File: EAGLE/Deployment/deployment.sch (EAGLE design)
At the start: 7 parts, among them J1 1935161, J2 1935161, J3 1935161, Q1 100V 14A

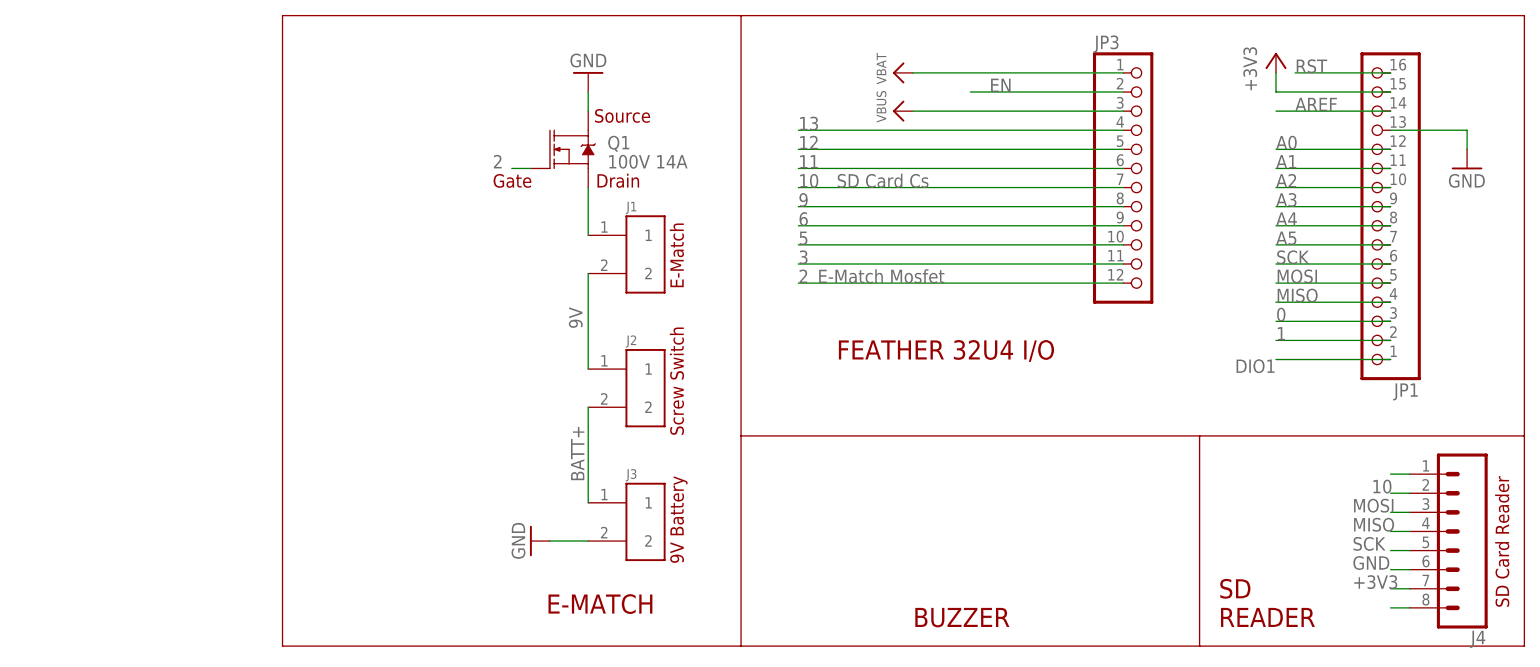
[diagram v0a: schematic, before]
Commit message: Fixed wiring of nichrome wire circit in the depolyment schematic
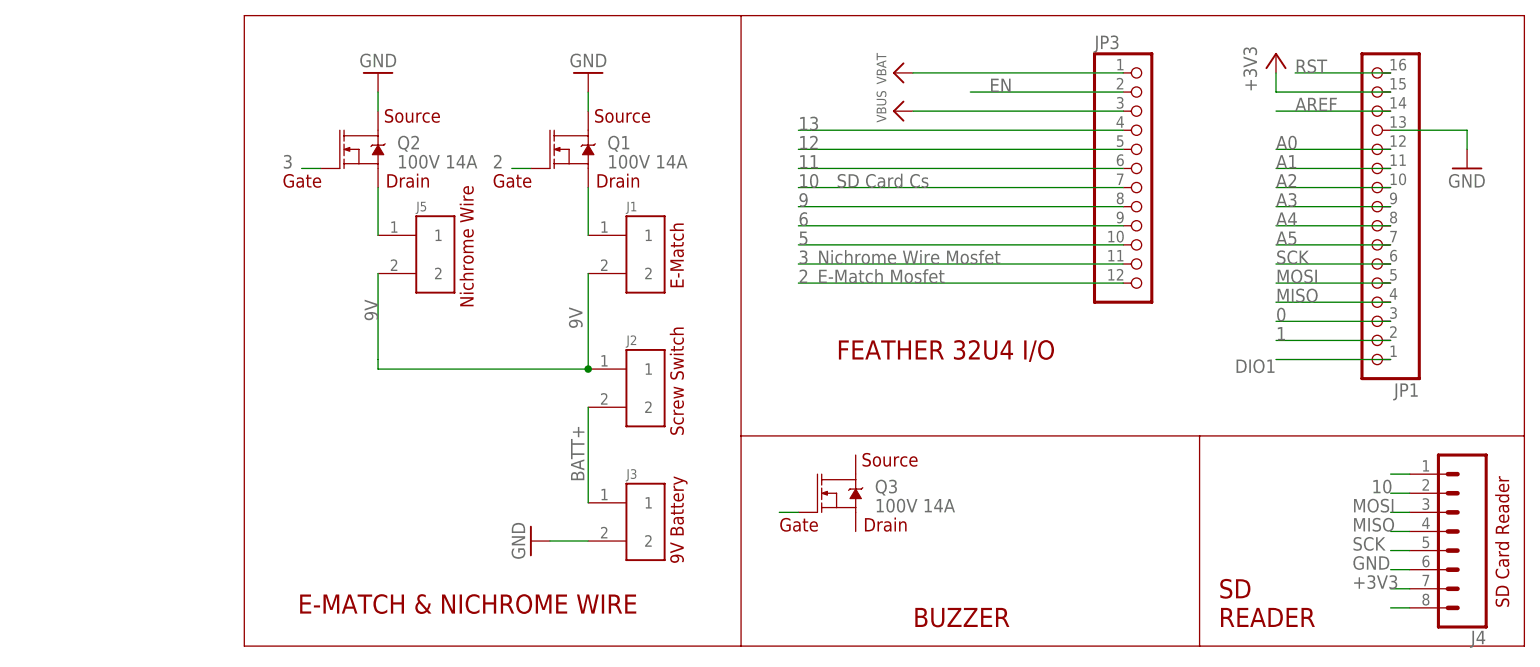
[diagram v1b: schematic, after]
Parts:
- added J5: 1935161, 1935161:1935161
- added Q2, Q3: 100V 14A, SparkFun-DiscreteSemi:MOSFET-NCH-FQP30N06L
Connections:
- new net 4: Q3.G
- new net N$2: J5.1, Q2.S
- net 3: now also Q2.G
- net 9V: now also J5.2
- net GND: now also Q2.D
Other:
- note added: "E-MATCH & NICHROME WIRE"
- note added: "Nichrome Wire"
- note added: "Nichrome Wire Mosfet"
- note removed: "E-MATCH"
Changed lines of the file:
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@@
 <?xml version="1.0" encoding="utf-8"?>
 <!DOCTYPE eagle SYSTEM "eagle.dtd">
-<eagle version="9.5.2">
+<eagle version="9.2.2">
 <drawing>
 <settings>
@@
 <part name="GND2" library="supply1" deviceset="GND" device=""/>
 <part name="J4" library="SparkFun-Connectors" library_urn="urn:adsk.eagle:library:513" deviceset="CONN_08" device="&quot;" package3d_urn="urn:adsk.eagle:package:38138/1"/>
+<part name="Q2" library="SparkFun-DiscreteSemi" library_urn="urn:adsk.eagle:library:514" deviceset="MOSFET-NCH" device="-FQP30N06L" package3d_urn="urn:adsk.eagle:package:38447/1" value="100V 14A"/>
+<part name="J5" library="1935161" deviceset="1935161" device="" value=""/>
+<part name="GND3" library="supply1" deviceset="GND" device=""/>
+<part name="Q3" library="SparkFun-DiscreteSemi" library_urn="urn:adsk.eagle:library:514" deviceset="MOSFET-NCH" device="-FQP30N06L" package3d_urn="urn:adsk.eagle:package:38447/1" value="100V 14A"/>
 </parts>
 <sheets>
@@
 <wire x1="127" y1="7.62" x2="127" y2="35.56" width="0.1524" layer="94"/>
 <wire x1="127" y1="7.62" x2="66.04" y2="7.62" width="0.1524" layer="94"/>
-<wire x1="66.04" y1="7.62" x2="5.08" y2="7.62" width="0.1524" layer="94"/>
-<wire x1="5.08" y1="7.62" x2="5.08" y2="91.44" width="0.1524" layer="94"/>
-<wire x1="5.08" y1="91.44" x2="66.04" y2="91.44" width="0.1524" layer="94"/>
+<wire x1="66.04" y1="7.62" x2="0" y2="7.62" width="0.1524" layer="94"/>
+<wire x1="0" y1="7.62" x2="0" y2="91.44" width="0.1524" layer="94"/>
+<wire x1="0" y1="91.44" x2="66.04" y2="91.44" width="0.1524" layer="94"/>
 <wire x1="66.04" y1="35.56" x2="66.04" y2="7.62" width="0.1524" layer="94"/>
-<text x="40.132" y="11.938" size="2.54" layer="94">E-MATCH</text>
+<text x="7.112" y="11.938" size="2.54" layer="94">E-MATCH &amp; NICHROME WIRE</text>
 <text x="78.74" y="45.72" size="2.54" layer="94">FEATHER 32U4 I/O</text>
 <text x="129.54" y="10.16" size="2.54" layer="94">SD
@@
 <text x="76.2" y="55.88" size="1.778" layer="95">E-Match Mosfet</text>
 <text x="78.74" y="68.58" size="1.778" layer="95">SD Card Cs</text>
+<text x="5.08" y="68.58" size="1.778" layer="94">Gate</text>
+<text x="18.542" y="77.216" size="1.778" layer="94">Source</text>
+<text x="18.796" y="68.58" size="1.778" layer="94">Drain</text>
+<text x="30.48" y="52.578" size="1.778" layer="94" rot="R90">Nichrome Wire</text>
+<text x="82.042" y="31.496" size="1.778" layer="94">Source</text>
+<text x="82.296" y="22.86" size="1.778" layer="94">Drain</text>
+<text x="71.12" y="22.86" size="1.778" layer="94">Gate</text>
+<text x="76.2" y="58.42" size="1.778" layer="95">Nichrome Wire Mosfet</text>
 </plain>
 <instances>
@@
 <attribute name="VALUE" x="165.1" y="35.306" size="1.778" layer="96" font="vector" rot="R180"/>
 <attribute name="NAME" x="165.1" y="9.652" size="1.778" layer="95" font="vector" rot="R180"/>
+</instance>
+<instance part="Q2" gate="NMOS" x="15.24" y="73.66" smashed="yes">
+<attribute name="NAME" x="20.32" y="73.66" size="1.778" layer="95" font="vector"/>
+<attribute name="VALUE" x="20.32" y="71.12" size="1.778" layer="96" font="vector"/>
+</instance>
+<instance part="J5" gate="G$1" x="25.4" y="59.69" smashed="yes">
+<attribute name="NAME" x="22.85451875" y="65.417340625" size="1.272740625" layer="95"/>
+<attribute name="VALUE" x="22.85191875" y="52.04576875" size="1.274040625" layer="96"/>
+</instance>
+<instance part="GND3" gate="1" x="17.78" y="83.82" smashed="yes" rot="R180">
+<attribute name="VALUE" x="20.32" y="86.36" size="1.778" layer="96" rot="R180"/>
+</instance>
+<instance part="Q3" gate="NMOS" x="78.74" y="27.94" smashed="yes">
+<attribute name="NAME" x="83.82" y="27.94" size="1.778" layer="95" font="vector"/>
+<attribute name="VALUE" x="83.82" y="25.4" size="1.778" layer="96" font="vector"/>
 </instance>
 </instances>
@@
 <label x="147.32" y="17.78" size="1.778" layer="95"/>
 </segment>
+<segment>
+<pinref part="GND3" gate="1" pin="GND"/>
+<pinref part="Q2" gate="NMOS" pin="D"/>
+<wire x1="17.78" y1="81.28" x2="17.78" y2="78.74" width="0.1524" layer="91"/>
+</segment>
 </net>
 <net name="MOSI" class="0">
@@
 <pinref part="JP3" gate="G$1" pin="11"/>
 </segment>
+<segment>
+<pinref part="Q2" gate="NMOS" pin="G"/>
+<wire x1="10.16" y1="71.12" x2="7.62" y2="71.12" width="0.1524" layer="91"/>
+<label x="5.08" y="71.12" size="1.778" layer="95"/>
+</segment>
 </net>
 <net name="EN" class="0">
@@
 <wire x1="45.72" y1="57.15" x2="45.72" y2="44.45" width="0.1524" layer="91"/>
 <label x="44.958" y="49.784" size="1.778" layer="95" rot="R90"/>
+<pinref part="J5" gate="G$1" pin="2"/>
+<wire x1="17.78" y1="57.15" x2="17.78" y2="45.72" width="0.1524" layer="91"/>
+<wire x1="45.72" y1="44.45" x2="17.78" y2="44.45" width="0.1524" layer="91"/>
+<wire x1="17.78" y1="44.45" x2="17.78" y2="45.72" width="0.1524" layer="91"/>
+<junction x="45.72" y="44.45"/>
+<label x="17.78" y="50.8" size="1.778" layer="95" rot="R90"/>
 </segment>
 </net>
@@
 </segment>
 </net>
+<net name="N$2" class="0">
+<segment>
+<pinref part="J5" gate="G$1" pin="1"/>
+<pinref part="Q2" gate="NMOS" pin="S"/>
+<wire x1="17.78" y1="62.23" x2="17.78" y2="68.58" width="0.1524" layer="91"/>
+</segment>
+</net>
+<net name="4" class="0">
+<segment>
+<pinref part="Q3" gate="NMOS" pin="G"/>
+<wire x1="73.66" y1="25.4" x2="71.12" y2="25.4" width="0.1524" layer="91"/>
+</segment>
+</net>

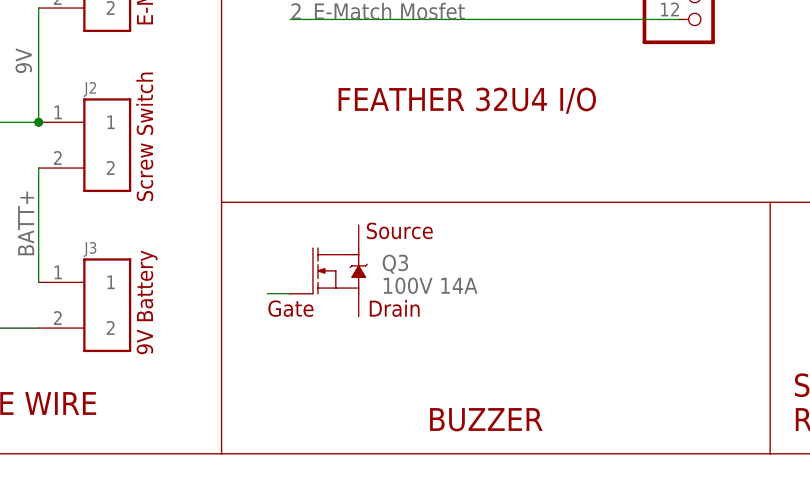
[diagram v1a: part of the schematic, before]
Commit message: Fixed issue with buzzer wiring
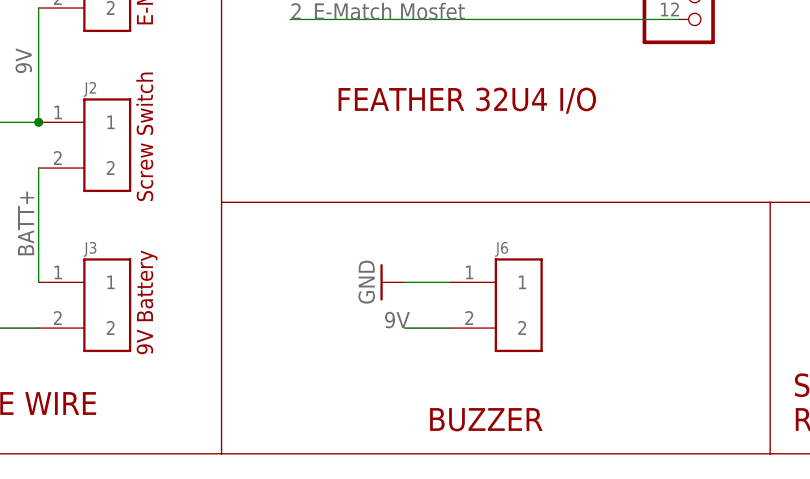
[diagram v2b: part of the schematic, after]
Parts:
- removed Q3: 100V 14A, SparkFun-DiscreteSemi:MOSFET-NCH-FQP30N06L
- added J6: 1935161, 1935161:1935161
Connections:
- removed net 4: Q3.G
- net 9V: now also J6.2
- net GND: now also J6.1
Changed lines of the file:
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@@
 <part name="J5" library="1935161" deviceset="1935161" device="" value=""/>
 <part name="GND3" library="supply1" deviceset="GND" device=""/>
-<part name="Q3" library="SparkFun-DiscreteSemi" library_urn="urn:adsk.eagle:library:514" deviceset="MOSFET-NCH" device="-FQP30N06L" package3d_urn="urn:adsk.eagle:package:38447/1" value="100V 14A"/>
+<part name="J6" library="1935161" deviceset="1935161" device="" value=""/>
+<part name="GND5" library="supply1" deviceset="GND" device=""/>
 </parts>
 <sheets>
@@
 <text x="18.796" y="68.58" size="1.778" layer="94">Drain</text>
 <text x="30.48" y="52.578" size="1.778" layer="94" rot="R90">Nichrome Wire</text>
-<text x="82.042" y="31.496" size="1.778" layer="94">Source</text>
-<text x="82.296" y="22.86" size="1.778" layer="94">Drain</text>
-<text x="71.12" y="22.86" size="1.778" layer="94">Gate</text>
 <text x="76.2" y="58.42" size="1.778" layer="95">Nichrome Wire Mosfet</text>
 </plain>
@@
 <attribute name="VALUE" x="20.32" y="86.36" size="1.778" layer="96" rot="R180"/>
 </instance>
-<instance part="Q3" gate="NMOS" x="78.74" y="27.94" smashed="yes">
-<attribute name="NAME" x="83.82" y="27.94" size="1.778" layer="95" font="vector"/>
-<attribute name="VALUE" x="83.82" y="25.4" size="1.778" layer="96" font="vector"/>
+<instance part="J6" gate="G$1" x="99.06" y="24.13" smashed="yes">
+<attribute name="NAME" x="96.51451875" y="29.857340625" size="1.272740625" layer="95"/>
+<attribute name="VALUE" x="96.51191875" y="16.48576875" size="1.274040625" layer="96"/>
+</instance>
+<instance part="GND5" gate="1" x="83.82" y="26.67" smashed="yes" rot="R270">
+<attribute name="VALUE" x="81.28" y="29.21" size="1.778" layer="96" rot="R270"/>
 </instance>
 </instances>
@@
 <pinref part="Q2" gate="NMOS" pin="D"/>
 <wire x1="17.78" y1="81.28" x2="17.78" y2="78.74" width="0.1524" layer="91"/>
+</segment>
+<segment>
+<pinref part="J6" gate="G$1" pin="1"/>
+<wire x1="91.44" y1="26.67" x2="86.36" y2="26.67" width="0.1524" layer="91"/>
+<pinref part="GND5" gate="1" pin="GND"/>
 </segment>
 </net>
@@
 <label x="17.78" y="50.8" size="1.778" layer="95" rot="R90"/>
 </segment>
+<segment>
+<pinref part="J6" gate="G$1" pin="2"/>
+<wire x1="91.44" y1="21.59" x2="86.36" y2="21.59" width="0.1524" layer="91"/>
+<label x="84.074" y="21.59" size="1.778" layer="95"/>
+</segment>
 </net>
 <net name="BATT+" class="0">
@@
 </segment>
 </net>
-<net name="4" class="0">
-<segment>
-<pinref part="Q3" gate="NMOS" pin="G"/>
-<wire x1="73.66" y1="25.4" x2="71.12" y2="25.4" width="0.1524" layer="91"/>
-</segment>
-</net>

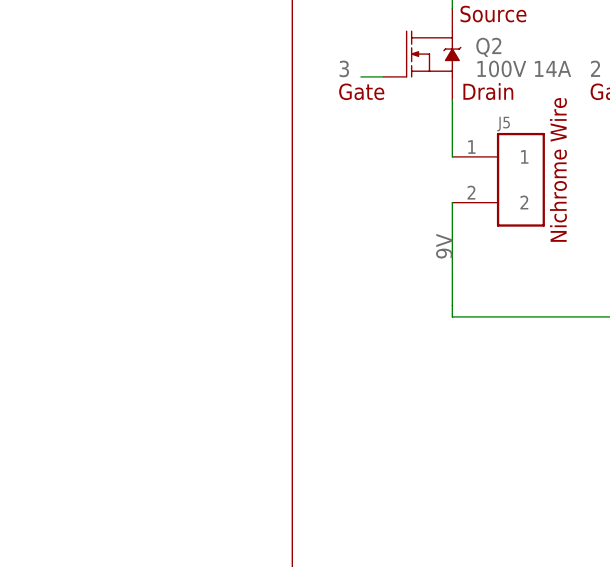
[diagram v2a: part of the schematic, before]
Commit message: starts full scale deployment circuitboard, neeeds design review and imu
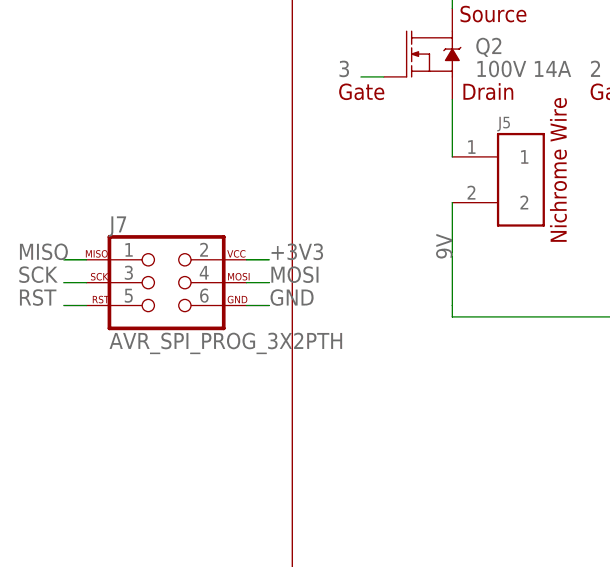
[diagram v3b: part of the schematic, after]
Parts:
- added J7: AVR_SPI_PROG_3X2PTH, SparkFun-Connectors:AVR_SPI_PROG_3X2PTH
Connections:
- net +3V3: now also J7.2
- net GND: now also J7.6
- net MISO: now also J7.1
- net MOSI: now also J7.4
- net RST: now also J7.5
- net SCK: now also J7.3
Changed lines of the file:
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@@
 <?xml version="1.0" encoding="utf-8"?>
 <!DOCTYPE eagle SYSTEM "eagle.dtd">
-<eagle version="9.2.2">
+<eagle version="9.5.1">
 <drawing>
 <settings>
@@
 <part name="J6" library="1935161" deviceset="1935161" device="" value=""/>
 <part name="GND5" library="supply1" deviceset="GND" device=""/>
+<part name="J7" library="SparkFun-Connectors" library_urn="urn:adsk.eagle:library:513" deviceset="AVR_SPI_PROG_3X2" device="PTH" package3d_urn="urn:adsk.eagle:package:38016/1"/>
 </parts>
 <sheets>
@@
 <attribute name="VALUE" x="81.28" y="29.21" size="1.778" layer="96" rot="R270"/>
 </instance>
+<instance part="J7" gate="G$1" x="-15.24" y="48.26" smashed="yes">
+<attribute name="NAME" x="-20.32" y="53.848" size="1.778" layer="95" font="vector"/>
+<attribute name="VALUE" x="-20.32" y="40.894" size="1.778" layer="96" font="vector"/>
+</instance>
 </instances>
 <busses>
@@
 <pinref part="GND5" gate="1" pin="GND"/>
 </segment>
+<segment>
+<pinref part="J7" gate="G$1" pin="6"/>
+<wire x1="-5.08" y1="45.72" x2="-2.54" y2="45.72" width="0.1524" layer="91"/>
+<label x="-2.54" y="45.72" size="1.778" layer="95"/>
+</segment>
 </net>
 <net name="MOSI" class="0">
@@
 <label x="147.32" y="25.4" size="1.778" layer="95"/>
 </segment>
+<segment>
+<pinref part="J7" gate="G$1" pin="4"/>
+<wire x1="-5.08" y1="48.26" x2="-2.54" y2="48.26" width="0.1524" layer="91"/>
+<label x="-2.54" y="48.26" size="1.778" layer="95"/>
+</segment>
 </net>
 <net name="MISO" class="0">
@@
 <label x="147.32" y="22.86" size="1.778" layer="95"/>
 </segment>
+<segment>
+<pinref part="J7" gate="G$1" pin="1"/>
+<wire x1="-22.86" y1="50.8" x2="-25.4" y2="50.8" width="0.1524" layer="91"/>
+<label x="-30.48" y="50.8" size="1.778" layer="95"/>
+</segment>
 </net>
 <net name="SCK" class="0">
@@
 <label x="147.32" y="20.32" size="1.778" layer="95"/>
 </segment>
+<segment>
+<pinref part="J7" gate="G$1" pin="3"/>
+<wire x1="-22.86" y1="48.26" x2="-25.4" y2="48.26" width="0.1524" layer="91"/>
+<label x="-30.48" y="48.26" size="1.778" layer="95"/>
+</segment>
 </net>
 <net name="RST" class="0">
@@
 <wire x1="152.4" y1="83.82" x2="139.7" y2="83.82" width="0.1524" layer="91"/>
 <label x="139.7" y="83.82" size="1.778" layer="95"/>
+</segment>
+<segment>
+<pinref part="J7" gate="G$1" pin="5"/>
+<wire x1="-22.86" y1="45.72" x2="-25.4" y2="45.72" width="0.1524" layer="91"/>
+<label x="-30.48" y="45.72" size="1.778" layer="95"/>
 </segment>
 </net>
@@
 <label x="147.32" y="15.24" size="1.778" layer="95"/>
 </segment>
-</net>
+<segment>
+<pinref part="J7" gate="G$1" pin="2"/>
+<wire x1="-5.08" y1="50.8" x2="-2.54" y2="50.8" width="0.1524" layer="91"/>
+<label x="-2.54" y="50.8" size="1.778" layer="95"/>
+</segment>
+</net>
